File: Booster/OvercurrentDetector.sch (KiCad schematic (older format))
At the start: 36 parts, among them U203 LM339, U501 LM338, U502 LM358, U503 NE555

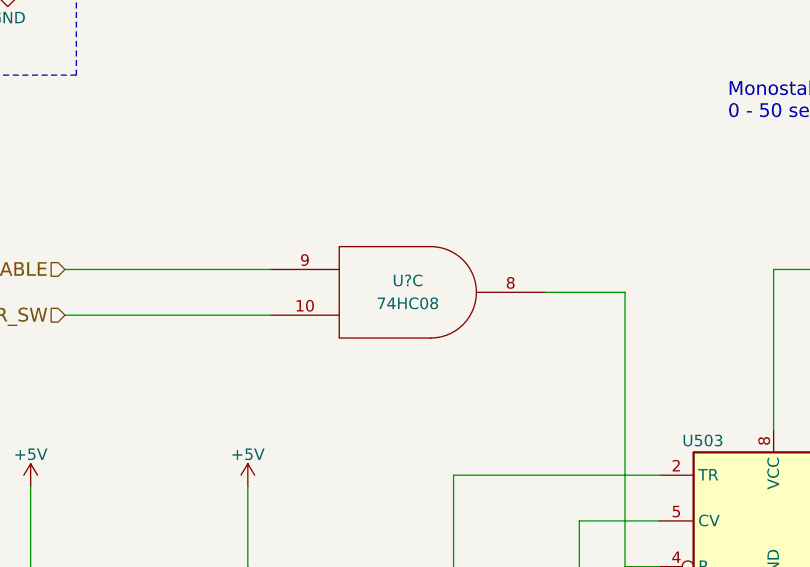
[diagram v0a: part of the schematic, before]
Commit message: Annotation, fix missing connection.
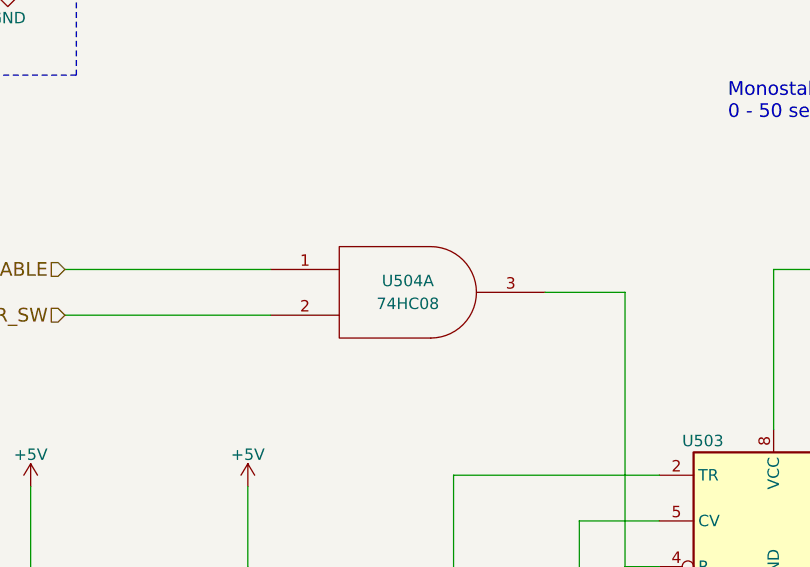
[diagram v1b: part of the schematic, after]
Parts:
- gave numbers to parts that had none: 1
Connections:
- net DCC_ENABLE: now also U504.1; no longer U504.9
- net MSTR_SW: now also U504.2; no longer U504.10
- net at U503.4 (R): now also U504.3; no longer U504.8
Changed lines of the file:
@@
 	2650 5750 2650 5450
-Wire Wire Line
-	2500 6800 2500 7100
 Wire Wire Line
 	2650 6650 2650 6550
@@
 Connection ~ 5200 5850
 $Comp
-L 74LS08 U?
-U 3 1 5A3EBEE8
+L 74LS08 U504
+U 1 1 5A3EBEE8
 P 6650 4100
-F 0 "U?" H 6650 4150 50  0000 C CNN
+F 0 "U504" H 6650 4150 50  0000 C CNN
 F 1 "74HC08" H 6650 4050 50  0000 C CNN
 F 2 "" H 6650 4100 50  0000 C CNN
 F 3 "" H 6650 4100 50  0000 C CNN
-	3    6650 4100
+	1    6650 4100
 	1    0    0    -1
 $EndComp
@@
 Wire Wire Line
 	5150 4000 6050 4000
+Wire Wire Line
+	2500 6800 2500 7100
 $EndSCHEMATC

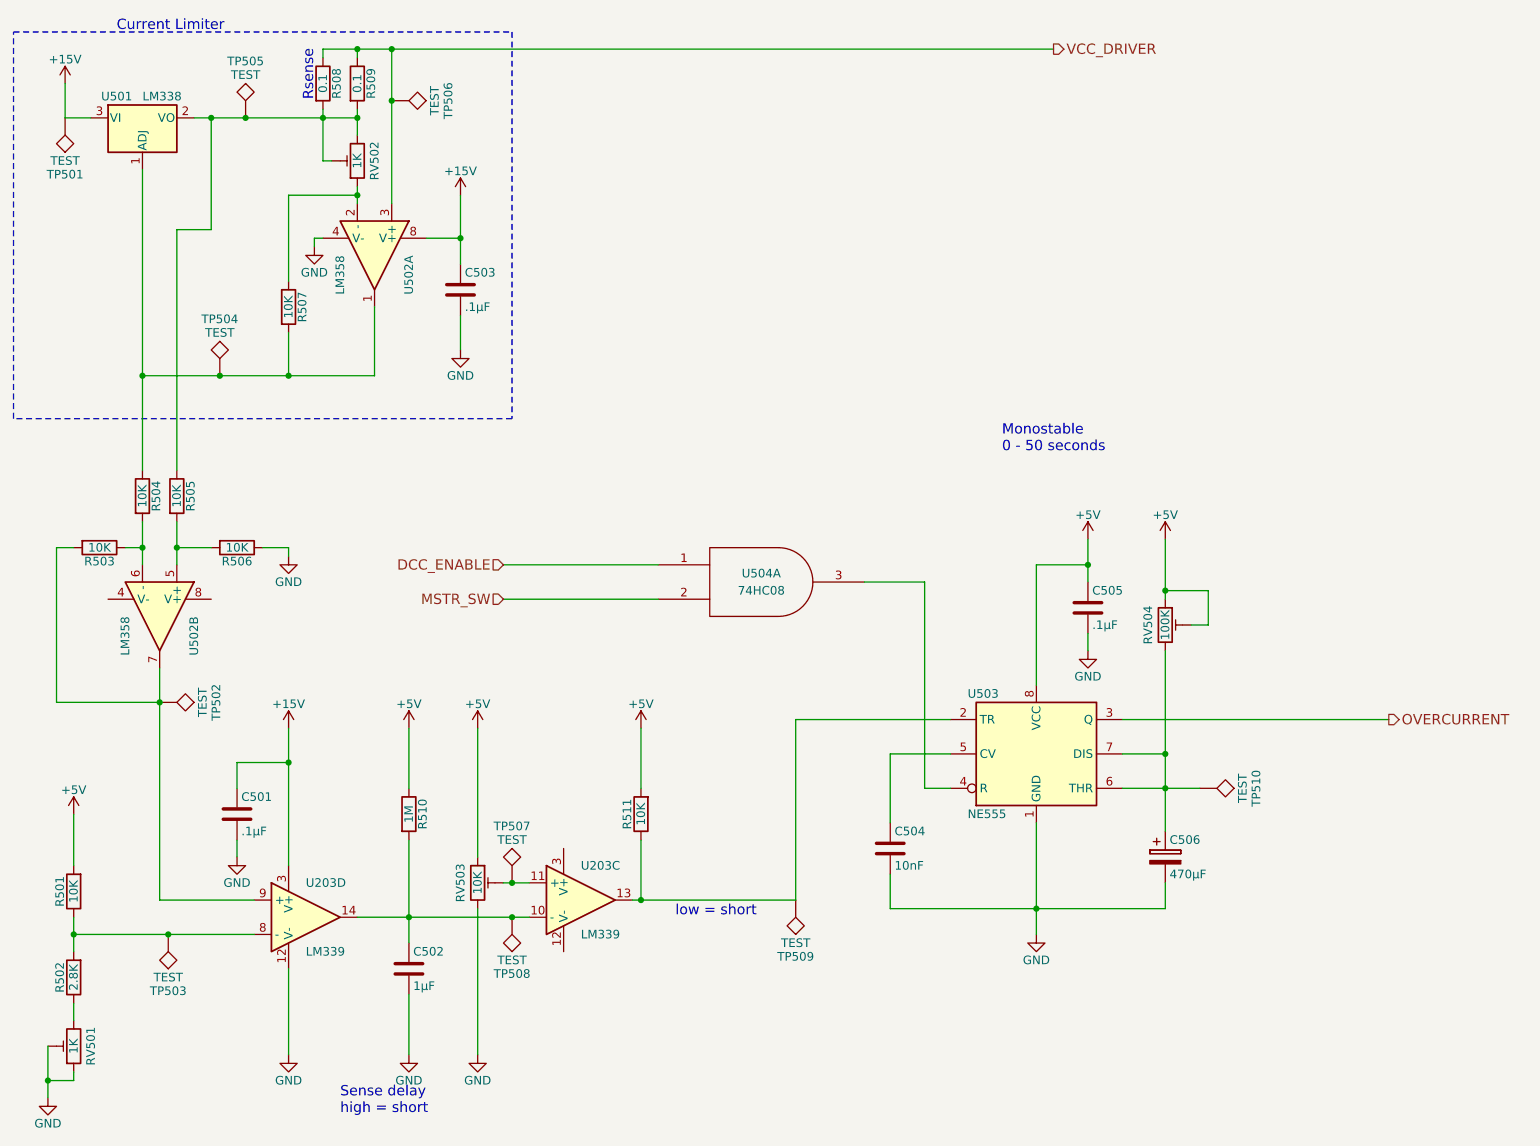
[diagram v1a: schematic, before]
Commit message: Assigned footprints & minor adjustments.
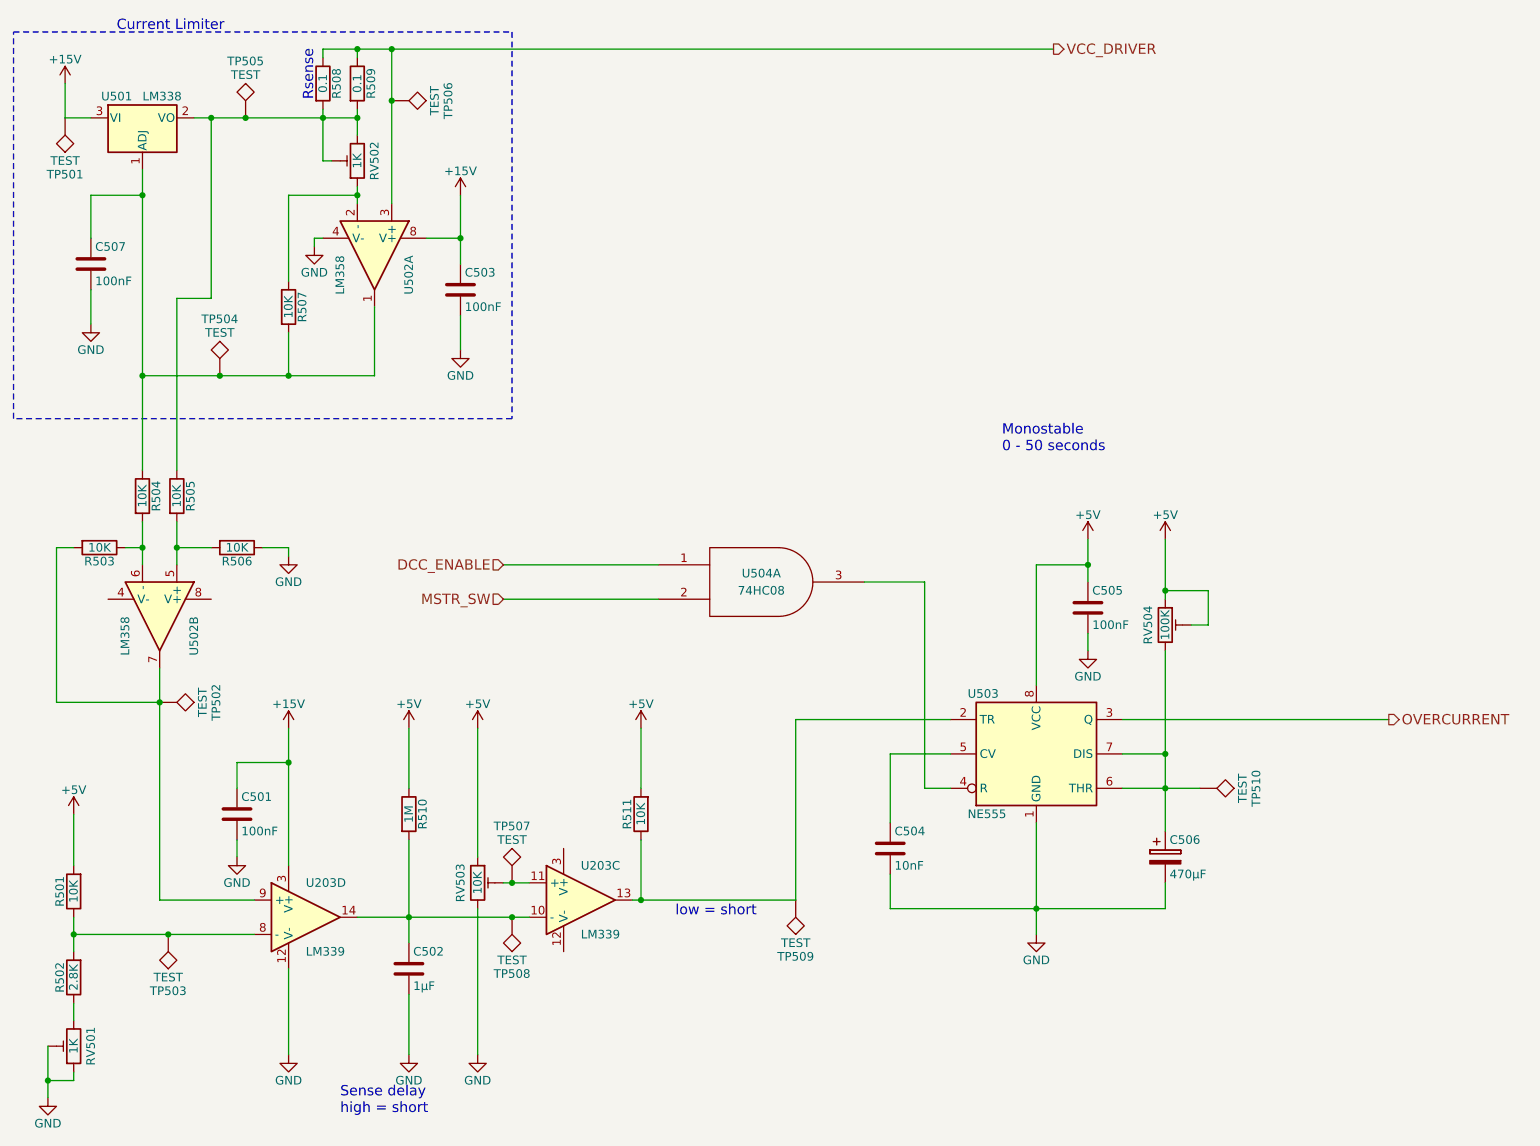
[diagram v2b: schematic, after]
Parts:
- added C507: 100nF, Capacitors_SMD:C_0805, symbol C
- C501, C503, C505: value .1µF -> 100nF; footprint (none) -> Capacitors_SMD:C_0805
- C502: footprint (none) -> Capacitors_THT:CP_Radial_D5.0mm_P2.50mm
- C504: footprint (none) -> Capacitors_SMD:C_0805
- C506: footprint (none) -> Capacitors_THT:CP_Radial_D10.0mm_P5.00mm
- R501, R502, R503, R504, R505, R506, R507, R508, R509, R510, R511: footprint (none) -> Resistors_SMD:R_0805
- RV501, RV502, RV503, RV504: footprint (none) -> Potentiometers:Potentiometer_Trimmer_Bourns_3296W
- TP501, TP502, TP503, TP504, TP505, TP506, TP507, TP508, TP509, TP510: footprint (none) -> Measurement_Points:Measurement_Point_Round-TH_Small
- U203, U504: footprint (none) -> SMD_Packages:SOIC-14_N
- U502, U503: footprint (none) -> SMD_Packages:SOIC-8-N
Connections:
- net GND: now also C507.2
- net at R504.1, R507.2, TP504.1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: now also C507.1
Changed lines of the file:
@@
 F 0 "R502" V 2730 6400 50  0000 C CNN
 F 1 "2.8K" V 2650 6400 50  0000 C CNN
-F 2 "" V 2580 6400 50  0000 C CNN
+F 2 "Resistors_SMD:R_0805" V 2580 6400 50  0001 C CNN
 F 3 "" H 2650 6400 50  0000 C CNN
 	1    2650 6400
@@
 F 0 "R501" V 2730 5900 50  0000 C CNN
 F 1 "10K" V 2650 5900 50  0000 C CNN
-F 2 "" V 2580 5900 50  0000 C CNN
+F 2 "Resistors_SMD:R_0805" V 2580 5900 50  0001 C CNN
 F 3 "" H 2650 5900 50  0000 C CNN
 	1    2650 5900
@@
 F 0 "R509" V 4380 1200 50  0000 C CNN
 F 1 "0.1" V 4300 1200 50  0000 C CNN
-F 2 "" V 4230 1200 50  0001 C CNN
+F 2 "Resistors_SMD:R_0805" V 4230 1200 50  0001 C CNN
 F 3 "" H 4300 1200 50  0001 C CNN
 	1    4300 1200
@@
 F 0 "R508" V 4180 1200 50  0000 C CNN
 F 1 "0.1" V 4100 1200 50  0000 C CNN
-F 2 "" V 4030 1200 50  0001 C CNN
+F 2 "Resistors_SMD:R_0805" V 4030 1200 50  0001 C CNN
 F 3 "" H 4100 1200 50  0001 C CNN
 	1    4100 1200
@@
 F 0 "U502" H 4400 2400 50  0000 L CNN
 F 1 "LM358" H 4400 2000 50  0000 L CNN
-F 2 "" H 4400 2200 50  0001 C CNN
+F 2 "SMD_Packages:SOIC-8-N" H 4400 2200 50  0001 C CNN
 F 3 "" H 4400 2200 50  0001 C CNN
 	1    4400 2200
@@
 F 0 "RV502" V 4200 1650 50  0000 C CNN
 F 1 "1K" V 4300 1650 50  0000 C CNN
-F 2 "" H 4300 1650 50  0001 C CNN
+F 2 "Potentiometers:Potentiometer_Trimmer_Bourns_3296W" H 4300 1650 50  0001 C CNN
 F 3 "" H 4300 1650 50  0001 C CNN
 	1    4300 1650
@@
 F 0 "R507" V 3980 2500 50  0000 C CNN
 F 1 "10K" V 3900 2500 50  0000 C CNN
-F 2 "" V 3830 2500 50  0000 C CNN
+F 2 "Resistors_SMD:R_0805" V 3830 2500 50  0001 C CNN
 F 3 "" H 3900 2500 50  0000 C CNN
 	1    3900 2500
@@
 P 4900 2400
 F 0 "C503" H 4925 2500 50  0000 L CNN
-F 1 ".1µF" H 4925 2300 50  0000 L CNN
-F 2 "" H 4938 2250 50  0001 C CNN
+F 1 "100nF" H 4925 2300 50  0000 L CNN
+F 2 "Capacitors_SMD:C_0805" H 4938 2250 50  0001 C CNN
 F 3 "" H 4900 2400 50  0001 C CNN
 	1    4900 2400
@@
 F 0 "U502" H 3150 4500 50  0000 L CNN
 F 1 "LM358" H 3150 4100 50  0000 L CNN
-F 2 "" H 3150 4300 50  0001 C CNN
+F 2 "SMD_Packages:SOIC-8-N" H 3150 4300 50  0001 C CNN
 F 3 "" H 3150 4300 50  0001 C CNN
 	2    3150 4300
@@
 F 0 "R504" V 3130 3600 50  0000 C CNN
 F 1 "10K" V 3050 3600 50  0000 C CNN
-F 2 "" V 2980 3600 50  0000 C CNN
+F 2 "Resistors_SMD:R_0805" V 2980 3600 50  0001 C CNN
 F 3 "" H 3050 3600 50  0000 C CNN
 	1    3050 3600
@@
 F 0 "R505" V 3330 3600 50  0000 C CNN
 F 1 "10K" V 3250 3600 50  0000 C CNN
-F 2 "" V 3180 3600 50  0000 C CNN
+F 2 "Resistors_SMD:R_0805" V 3180 3600 50  0001 C CNN
 F 3 "" H 3250 3600 50  0000 C CNN
 	1    3250 3600
@@
 F 0 "R506" V 3680 3900 50  0000 C CNN
 F 1 "10K" V 3600 3900 50  0000 C CNN
-F 2 "" V 3530 3900 50  0000 C CNN
+F 2 "Resistors_SMD:R_0805" V 3530 3900 50  0001 C CNN
 F 3 "" H 3600 3900 50  0000 C CNN
 	1    3600 3900
@@
 F 0 "R503" V 2880 3900 50  0000 C CNN
 F 1 "10K" V 2800 3900 50  0000 C CNN
-F 2 "" V 2730 3900 50  0000 C CNN
+F 2 "Resistors_SMD:R_0805" V 2730 3900 50  0001 C CNN
 F 3 "" H 2800 3900 50  0000 C CNN
 	1    2800 3900
@@
 F 0 "U203" H 4000 6250 50  0000 L CNN
 F 1 "LM339" H 4000 5850 50  0000 L CNN
-F 2 "" H 3950 6150 50  0000 C CNN
+F 2 "SMD_Packages:SOIC-14_N" H 3950 6150 50  0001 C CNN
 F 3 "" H 4050 6250 50  0000 C CNN
 	4    4000 6050
@@
 F 0 "RV501" V 2550 6800 50  0000 C CNN
 F 1 "1K" V 2650 6800 50  0000 C CNN
-F 2 "" H 2650 6800 50  0001 C CNN
+F 2 "Potentiometers:Potentiometer_Trimmer_Bourns_3296W" H 2650 6800 50  0001 C CNN
 F 3 "" H 2650 6800 50  0001 C CNN
 	1    2650 6800
@@
 F 0 "C502" H 4625 6450 50  0000 L CNN
 F 1 "1µF" H 4625 6250 50  0000 L CNN
-F 2 "" H 4638 6200 50  0001 C CNN
+F 2 "Capacitors_THT:CP_Radial_D5.0mm_P2.50mm" H 4638 6200 50  0001 C CNN
 F 3 "" H 4600 6350 50  0001 C CNN
 	1    4600 6350
@@
 F 0 "R510" V 4680 5450 50  0000 C CNN
 F 1 "1M" V 4600 5450 50  0000 C CNN
-F 2 "" V 4530 5450 50  0000 C CNN
+F 2 "Resistors_SMD:R_0805" V 4530 5450 50  0001 C CNN
 F 3 "" H 4600 5450 50  0000 C CNN
 	1    4600 5450
@@
 F 0 "U203" H 5600 6150 50  0000 L CNN
 F 1 "LM339" H 5600 5750 50  0000 L CNN
-F 2 "" H 5550 6050 50  0000 C CNN
+F 2 "SMD_Packages:SOIC-14_N" H 5550 6050 50  0001 C CNN
 F 3 "" H 5650 6150 50  0000 C CNN
 	3    5600 5950
@@
 F 0 "RV503" V 4900 5850 50  0000 C CNN
 F 1 "10K" V 5000 5850 50  0000 C CNN
-F 2 "" H 5000 5850 50  0001 C CNN
+F 2 "Potentiometers:Potentiometer_Trimmer_Bourns_3296W" H 5000 5850 50  0001 C CNN
 F 3 "" H 5000 5850 50  0001 C CNN
 	1    5000 5850
@@
 P 3600 5450
 F 0 "C501" H 3625 5550 50  0000 L CNN
-F 1 ".1µF" H 3625 5350 50  0000 L CNN
-F 2 "" H 3638 5300 50  0001 C CNN
+F 1 "100nF" H 3625 5350 50  0000 L CNN
+F 2 "Capacitors_SMD:C_0805" H 3638 5300 50  0001 C CNN
 F 3 "" H 3600 5450 50  0001 C CNN
 	1    3600 5450
@@
 F 0 "TP505" H 3650 1700 50  0000 C BNN
 F 1 "TEST" H 3650 1650 50  0000 C CNN
-F 2 "" H 3650 1400 50  0001 C CNN
+F 2 "Measurement_Points:Measurement_Point_Round-TH_Small" H 3650 1400 50  0001 C CNN
 F 3 "" H 3650 1400 50  0001 C CNN
 	1    3650 1400
@@
 F 0 "TP504" H 3500 3200 50  0000 C BNN
 F 1 "TEST" H 3500 3150 50  0000 C CNN
-F 2 "" H 3500 2900 50  0001 C CNN
+F 2 "Measurement_Points:Measurement_Point_Round-TH_Small" H 3500 2900 50  0001 C CNN
 F 3 "" H 3500 2900 50  0001 C CNN
 	1    3500 2900
@@
 F 0 "TP502" H 3150 5100 50  0000 C BNN
 F 1 "TEST" H 3150 5050 50  0000 C CNN
-F 2 "" H 3150 4800 50  0001 C CNN
+F 2 "Measurement_Points:Measurement_Point_Round-TH_Small" H 3150 4800 50  0001 C CNN
 F 3 "" H 3150 4800 50  0001 C CNN
 	1    3150 4800
@@
 F 0 "TP503" H 3200 6450 50  0000 C BNN
 F 1 "TEST" H 3200 6400 50  0000 C CNN
-F 2 "" H 3200 6150 50  0001 C CNN
+F 2 "Measurement_Points:Measurement_Point_Round-TH_Small" H 3200 6150 50  0001 C CNN
 F 3 "" H 3200 6150 50  0001 C CNN
 	1    3200 6150
@@
 F 0 "TP507" H 5200 6150 50  0000 C BNN
 F 1 "TEST" H 5200 6100 50  0000 C CNN
-F 2 "" H 5200 5850 50  0001 C CNN
+F 2 "Measurement_Points:Measurement_Point_Round-TH_Small" H 5200 5850 50  0001 C CNN
 F 3 "" H 5200 5850 50  0001 C CNN
 	1    5200 5850
@@
 F 0 "TP508" H 5200 6350 50  0000 C BNN
 F 1 "TEST" H 5200 6300 50  0000 C CNN
-F 2 "" H 5200 6050 50  0001 C CNN
+F 2 "Measurement_Points:Measurement_Point_Round-TH_Small" H 5200 6050 50  0001 C CNN
 F 3 "" H 5200 6050 50  0001 C CNN
 	1    5200 6050
@@
 F 0 "TP506" H 4500 1600 50  0000 C BNN
 F 1 "TEST" H 4500 1550 50  0000 C CNN
-F 2 "" H 4500 1300 50  0001 C CNN
+F 2 "Measurement_Points:Measurement_Point_Round-TH_Small" H 4500 1300 50  0001 C CNN
 F 3 "" H 4500 1300 50  0001 C CNN
 	1    4500 1300
@@
 F 0 "TP501" H 2600 1700 50  0000 C BNN
 F 1 "TEST" H 2600 1650 50  0000 C CNN
-F 2 "" H 2600 1400 50  0001 C CNN
+F 2 "Measurement_Points:Measurement_Point_Round-TH_Small" H 2600 1400 50  0001 C CNN
 F 3 "" H 2600 1400 50  0001 C CNN
 	1    2600 1400
@@
 F 0 "U503" H 7850 5450 50  0000 L CNN
 F 1 "NE555" H 7850 4750 50  0000 L CNN
-F 2 "" H 8250 5100 50  0000 C CNN
+F 2 "SMD_Packages:SOIC-8-N" H 8250 5100 50  0001 C CNN
 F 3 "" H 8250 5100 50  0000 C CNN
 	1    8250 5100
@@
 F 0 "R511" V 6030 5450 50  0000 C CNN
 F 1 "10K" V 5950 5450 50  0000 C CNN
-F 2 "" V 5880 5450 50  0000 C CNN
+F 2 "Resistors_SMD:R_0805" V 5880 5450 50  0001 C CNN
 F 3 "" H 5950 5450 50  0000 C CNN
 	1    5950 5450
@@
 F 0 "C504" H 7425 5750 50  0000 L CNN
 F 1 "10nF" H 7425 5550 50  0000 L CNN
-F 2 "" H 7438 5500 50  0001 C CNN
+F 2 "Capacitors_SMD:C_0805" H 7438 5500 50  0001 C CNN
 F 3 "" H 7400 5650 50  0001 C CNN
 	1    7400 5650
@@
 P 8550 4250
 F 0 "C505" H 8575 4350 50  0000 L CNN
-F 1 ".1µF" H 8575 4150 50  0000 L CNN
-F 2 "" H 8588 4100 50  0001 C CNN
+F 1 "100nF" H 8575 4150 50  0000 L CNN
+F 2 "Capacitors_SMD:C_0805" H 8588 4100 50  0001 C CNN
 F 3 "" H 8550 4250 50  0001 C CNN
 	1    8550 4250
@@
 F 0 "RV504" V 8900 4350 50  0000 C CNN
 F 1 "100K" V 9000 4350 50  0000 C CNN
-F 2 "" H 9000 4350 50  0001 C CNN
+F 2 "Potentiometers:Potentiometer_Trimmer_Bourns_3296W" H 9000 4350 50  0001 C CNN
 F 3 "" H 9000 4350 50  0001 C CNN
 	1    9000 4350
@@
 	3250 3750 3250 4000
 Wire Wire Line
-	3250 2050 3250 3450
-Wire Wire Line
-	3250 2050 3450 2050
-Wire Wire Line
-	3450 2050 3450 1400
+	3250 2450 3250 3450
+Wire Wire Line
+	3250 2450 3450 2450
+Wire Wire Line
+	3450 2450 3450 1400
 Connection ~ 3450 1400
 Connection ~ 3250 3900
@@
 F 0 "C506" H 9025 5800 50  0000 L CNN
 F 1 "470µF" H 9025 5600 50  0000 L CNN
-F 2 "" H 9038 5550 50  0000 C CNN
+F 2 "Capacitors_THT:CP_Radial_D10.0mm_P5.00mm" H 9038 5550 50  0001 C CNN
 F 3 "" H 9000 5700 50  0000 C CNN
 	1    9000 5700
@@
 F 0 "TP509" H 6850 6250 50  0000 C BNN
 F 1 "TEST" H 6850 6200 50  0000 C CNN
-F 2 "" H 6850 5950 50  0001 C CNN
+F 2 "Measurement_Points:Measurement_Point_Round-TH_Small" H 6850 5950 50  0001 C CNN
 F 3 "" H 6850 5950 50  0001 C CNN
 	1    6850 5950
@@
 F 0 "TP510" H 9200 5600 50  0000 C BNN
 F 1 "TEST" H 9200 5550 50  0000 C CNN
-F 2 "" H 9200 5300 50  0001 C CNN
+F 2 "Measurement_Points:Measurement_Point_Round-TH_Small" H 9200 5300 50  0001 C CNN
 F 3 "" H 9200 5300 50  0001 C CNN
 	1    9200 5300
@@
 F 0 "U504" H 6650 4150 50  0000 C CNN
 F 1 "74HC08" H 6650 4050 50  0000 C CNN
-F 2 "" H 6650 4100 50  0000 C CNN
+F 2 "SMD_Packages:SOIC-14_N" H 6650 4100 50  0001 C CNN
 F 3 "" H 6650 4100 50  0000 C CNN
 	1    6650 4100
@@
 Wire Wire Line
 	2500 6800 2500 7100
+Connection ~ 3050 1850
+Wire Wire Line
+	3050 1850 2750 1850
+Wire Wire Line
+	2750 1850 2750 2100
+$Comp
+L C C507
+U 1 1 5A413028
+P 2750 2250
+F 0 "C507" H 2775 2350 50  0000 L CNN
+F 1 "100nF" H 2775 2150 50  0000 L CNN
+F 2 "Capacitors_SMD:C_0805" H 2788 2100 50  0001 C CNN
+F 3 "" H 2750 2250 50  0001 C CNN
+	1    2750 2250
+	1    0    0    -1
+$EndComp
+Wire Wire Line
+	2750 2400 2750 2600
+$Comp
+L GND #PWR038
+U 1 1 5A413136
+P 2750 2600
+F 0 "#PWR038" H 2750 2350 50  0001 C CNN
+F 1 "GND" H 2750 2450 50  0000 C CNN
+F 2 "" H 2750 2600 50  0000 C CNN
+F 3 "" H 2750 2600 50  0000 C CNN
+	1    2750 2600
+	1    0    0    -1
+$EndComp
 $EndSCHEMATC

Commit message: Started working on the PCB layout. Just getting a rough idea for now.
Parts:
- U501: footprint TO_SOT_Packages_THT:TO-220_Vertical -> Trainiot:TO-220-3_Vertical_Single_Pin_Heatshield
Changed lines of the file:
@@
 F 0 "U501" H 2900 1525 50  0000 C CNN
 F 1 "LM338" H 3050 1525 50  0000 L CNN
-F 2 "TO_SOT_Packages_THT:TO-220_Vertical" H 3050 1650 50  0001 C CIN
+F 2 "Trainiot:TO-220-3_Vertical_Single_Pin_Heatshield" H 3050 1650 50  0001 C CIN
 F 3 "" H 3050 1400 50  0001 C CNN
 	1    3050 1400
